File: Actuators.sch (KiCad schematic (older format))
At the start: 16 parts, among them J1 SERVO PWR, M1 Motor_Servo, M2 Motor_Servo, M3 Pump 1, M4 Pump 2, U6 DRV8847_TSSOP

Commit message: Upadate footprints, rough arrangement
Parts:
- removed L1: Solenoid 1, Connector_PinHeader_2.54mm:PinHeader_1x02_P2.54mm_Vertical, symbol Device:Electromagnetic_Actor
- removed L2: Solenoid 2, Connector_PinHeader_2.54mm:PinHeader_1x02_P2.54mm_Vertical, symbol Device:Electromagnetic_Actor
- removed M3: Pump 1, Connector_PinHeader_2.54mm:PinHeader_1x02_P2.54mm_Vertical, symbol Motor:Motor_DC
- removed M4: Pump 2, Connector_PinHeader_2.54mm:PinHeader_1x02_P2.54mm_Vertical, symbol Motor:Motor_DC
- added J3: Actuator1, Connector_Molex:Molex_PicoBlade_53261-0471_1x04-1MP_P1.25mm_Horizontal, symbol Connector_Generic:Conn_01x04
- added J4: Actuator2, Connector_Molex:Molex_PicoBlade_53261-0471_1x04-1MP_P1.25mm_Horizontal, symbol Connector_Generic:Conn_01x04
- C19: footprint Capacitor_THT:CP_Radial_D6.3mm_P2.50mm -> Capacitor_SMD:CP_Elec_5x5.8
- J1: value SERVO PWR -> SERVO DCDC 5V; footprint Connector_PinHeader_2.54mm:PinHeader_1x02_P2.54mm_Vertical -> Connector_PinHeader_2.54mm:PinHeader_1x03_P2.54mm_Vertical; symbol Connector_Generic:Conn_01x02 -> Connector_Generic:Conn_01x03
- M1, M2: footprint Connector_PinHeader_2.54mm:PinHeader_1x03_P2.54mm_Horizontal -> Connector_Molex:Molex_PicoBlade_53261-0371_1x03-1MP_P1.25mm_Horizontal
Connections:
- net +BATT: now also J1.1 (Pin_1)
- net GND: now also J3.2 (Pin_2), J3.4 (Pin_4), J4.2 (Pin_2), J4.4 (Pin_4)
- net at D3.1 (K), U6.2 (OUT1): now also J3.1 (Pin_1)
- net at D5.1 (K), U6.7 (OUT3): now also J4.1 (Pin_1)
- net at C17.1, M1.2 (+), M2.2 (+): now also J1.3 (Pin_3); no longer J1.1 (Pin_1)
- net at D4.1 (K), U6.4 (OUT2): now also J3.3 (Pin_3)
- net at D6.1 (K), U6.5 (OUT4): now also J4.3 (Pin_3)
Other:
- note added: "Pump 1"
- note added: "Pump 2"
- note added: "Solenoid 1"
- note added: "Solenoid 2"
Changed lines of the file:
@@
 Text HLabel 3850 2950 0    50   Input ~ 0
 SOLENOID_IN2
-$Comp
-L Motor:Motor_Servo M1
-U 1 1 5E37BD0B
-P 5000 5350
-F 0 "M1" H 5332 5415 50  0000 L CNN
-F 1 "Motor_Servo" H 5332 5324 50  0000 L CNN
-F 2 "Connector_PinHeader_2.54mm:PinHeader_1x03_P2.54mm_Horizontal" H 5000 5160 50  0001 C CNN
-F 3 "http://forums.parallax.com/uploads/attachments/46831/74481.png" H 5000 5160 50  0001 C CNN
-	1    5000 5350
-	1    0    0    -1
-$EndComp
-$Comp
-L Motor:Motor_Servo M2
-U 1 1 5E38464C
-P 5000 5900
-F 0 "M2" H 5332 5965 50  0000 L CNN
-F 1 "Motor_Servo" H 5332 5874 50  0000 L CNN
-F 2 "Connector_PinHeader_2.54mm:PinHeader_1x03_P2.54mm_Horizontal" H 5000 5710 50  0001 C CNN
-F 3 "http://forums.parallax.com/uploads/attachments/46831/74481.png" H 5000 5710 50  0001 C CNN
-	1    5000 5900
-	1    0    0    -1
-$EndComp
 Text HLabel 3850 2750 0    50   Input ~ 0
 SOLENOID_IN1
@@
 $EndComp
 $Comp
-L Connector_Generic:Conn_01x02 J1
+L Connector_Generic:Conn_01x03 J1
 U 1 1 5E3C2833
-P 2600 5350
-F 0 "J1" H 2518 5567 50  0000 C CNN
-F 1 "SERVO PWR" H 2518 5476 50  0000 C CNN
-F 2 "Connector_PinHeader_2.54mm:PinHeader_1x02_P2.54mm_Vertical" H 2600 5350 50  0001 C CNN
-F 3 "~" H 2600 5350 50  0001 C CNN
-	1    2600 5350
+P 2600 5250
+F 0 "J1" H 2600 5450 50  0000 C CNN
+F 1 "SERVO DCDC 5V" H 2600 5000 50  0000 C CNN
+F 2 "Connector_PinHeader_2.54mm:PinHeader_1x03_P2.54mm_Vertical" H 2600 5250 50  0001 C CNN
+F 3 "~" H 2600 5250 50  0001 C CNN
+	1    2600 5250
 	-1   0    0    -1
 $EndComp
 Wire Wire Line
-	2800 5450 3050 5450
-Wire Wire Line
-	3050 5450 3050 5650
+	2800 5250 3050 5250
+Wire Wire Line
+	3050 5250 3050 5650
 Wire Wire Line
 	3050 5650 3350 5650
@@
 	1    0    0    -1
 $EndComp
-$Comp
-L Motor:Motor_DC M3
-U 1 1 5E248EAA
-P 7450 2150
-F 0 "M3" V 7250 2100 50  0000 C CNN
-F 1 "Pump 1" V 7650 2100 39  0000 C CNN
-F 2 "Connector_PinHeader_2.54mm:PinHeader_1x02_P2.54mm_Vertical" H 7450 2060 50  0001 C CNN
-F 3 "~" H 7450 2060 50  0001 C CNN
-	1    7450 2150
-	1    0    0    -1
-$EndComp
-$Comp
-L Motor:Motor_DC M4
-U 1 1 5E2BC872
-P 7450 3900
-F 0 "M4" V 7250 3850 50  0000 C CNN
-F 1 "Pump 2" V 7650 3850 39  0000 C CNN
-F 2 "Connector_PinHeader_2.54mm:PinHeader_1x02_P2.54mm_Vertical" H 7450 3810 50  0001 C CNN
-F 3 "~" H 7450 3810 50  0001 C CNN
-	1    7450 3900
-	1    0    0    -1
-$EndComp
 Wire Wire Line
 	5250 2650 6600 2650
@@
 Connection ~ 7000 1950
 Wire Wire Line
-	7000 1950 7450 1950
-Wire Wire Line
 	7000 2350 7000 2450
 Wire Wire Line
@@
 Connection ~ 7000 3700
 Wire Wire Line
-	7000 3700 7450 3700
-Wire Wire Line
 	7000 4100 7000 4200
 Wire Wire Line
@@
 	7000 4600 7000 4500
 Connection ~ 7000 4500
-Wire Wire Line
-	7000 4500 7450 4500
 Wire Wire Line
 	7000 4900 7000 5000
@@
 	7000 3150 7000 3250
 Wire Wire Line
-	7000 2750 7450 2750
-Wire Wire Line
 	5250 2750 7000 2750
 Connection ~ 7000 2750
 Wire Wire Line
 	7000 2850 7000 2750
-$Comp
-L Device:Electromagnetic_Actor L1
-U 1 1 5E5DF558
-P 7450 3050
-F 0 "L1" H 7580 3146 50  0000 L CNN
-F 1 "Solenoid 1" H 7580 3055 50  0000 L CNN
-F 2 "Connector_PinHeader_2.54mm:PinHeader_1x02_P2.54mm_Vertical" V 7425 3150 50  0001 C CNN
-F 3 "~" V 7425 3150 50  0001 C CNN
-	1    7450 3050
-	1    0    0    -1
-$EndComp
-Wire Wire Line
-	7450 2750 7450 2850
-Wire Wire Line
-	7450 3150 7450 3250
-$Comp
-L Device:Electromagnetic_Actor L2
-U 1 1 5E5E309E
-P 7450 4800
-F 0 "L2" H 7580 4896 50  0000 L CNN
-F 1 "Solenoid 2" H 7580 4805 50  0000 L CNN
-F 2 "Connector_PinHeader_2.54mm:PinHeader_1x02_P2.54mm_Vertical" V 7425 4900 50  0001 C CNN
-F 3 "~" V 7425 4900 50  0001 C CNN
-	1    7450 4800
-	1    0    0    -1
-$EndComp
-Wire Wire Line
-	7450 4500 7450 4600
-Wire Wire Line
-	7450 4900 7450 5000
-Text Notes 7600 2650 0    50   ~ 0
+Text Notes 7650 2050 0    50   ~ 0
 Actuator 1\n(1A max)
 Wire Notes Line
@@
 Wire Notes Line
 	6800 3600 8050 3600
-Text Notes 7600 4400 0    50   ~ 0
+Text Notes 7600 3800 0    50   ~ 0
 Actuator 2\n(1A max)
 $Comp
@@
 F 0 "C19" H 5200 2250 50  0000 L CNN
 F 1 "22uF" H 5200 2150 50  0000 L CNN
-F 2 "Capacitor_THT:CP_Radial_D6.3mm_P2.50mm" H 5538 2050 50  0001 C CNN
+F 2 "Capacitor_SMD:CP_Elec_5x5.8" H 5538 2050 50  0001 C CNN
 F 3 "~" H 5500 2200 50  0001 C CNN
 	1    5500 2200
@@
 Text Notes 5200 2400 0    50   ~ 0
 ≥16V
+$Comp
+L Motor:Motor_Servo M2
+U 1 1 5E38464C
+P 5000 5900
+F 0 "M2" H 5332 5965 50  0000 L CNN
+F 1 "Motor_Servo" H 5332 5874 50  0000 L CNN
+F 2 "Connector_Molex:Molex_PicoBlade_53261-0371_1x03-1MP_P1.25mm_Horizontal" H 5000 5710 50  0001 C CNN
+F 3 "http://forums.parallax.com/uploads/attachments/46831/74481.png" H 5000 5710 50  0001 C CNN
+	1    5000 5900
+	1    0    0    -1
+$EndComp
+$Comp
+L Motor:Motor_Servo M1
+U 1 1 5E37BD0B
+P 5000 5350
+F 0 "M1" H 5332 5415 50  0000 L CNN
+F 1 "Motor_Servo" H 5332 5324 50  0000 L CNN
+F 2 "Connector_Molex:Molex_PicoBlade_53261-0371_1x03-1MP_P1.25mm_Horizontal" H 5000 5160 50  0001 C CNN
+F 3 "http://forums.parallax.com/uploads/attachments/46831/74481.png" H 5000 5160 50  0001 C CNN
+	1    5000 5350
+	1    0    0    -1
+$EndComp
+$Comp
+L Connector_Generic:Conn_01x04 J3
+U 1 1 5E485C32
+P 7750 2650
+F 0 "J3" H 7830 2642 50  0000 L CNN
+F 1 "Actuator1" H 7830 2551 50  0000 L CNN
+F 2 "Connector_Molex:Molex_PicoBlade_53261-0471_1x04-1MP_P1.25mm_Horizontal" H 7750 2650 50  0001 C CNN
+F 3 "~" H 7750 2650 50  0001 C CNN
+	1    7750 2650
+	1    0    0    -1
+$EndComp
+$Comp
+L Connector_Generic:Conn_01x04 J4
+U 1 1 5E486381
+P 7750 4400
+F 0 "J4" H 7830 4392 50  0000 L CNN
+F 1 "Actuator2" H 7830 4301 50  0000 L CNN
+F 2 "Connector_Molex:Molex_PicoBlade_53261-0471_1x04-1MP_P1.25mm_Horizontal" H 7750 4400 50  0001 C CNN
+F 3 "~" H 7750 4400 50  0001 C CNN
+	1    7750 4400
+	1    0    0    -1
+$EndComp
+Wire Wire Line
+	7550 1950 7550 2550
+Wire Wire Line
+	7000 1950 7550 1950
+Wire Wire Line
+	7450 2450 7450 2650
+Wire Wire Line
+	7450 2650 7550 2650
+Wire Wire Line
+	7000 2750 7550 2750
+Wire Wire Line
+	7550 2850 7450 2850
+Wire Wire Line
+	7450 2850 7450 3250
+Wire Wire Line
+	7000 4500 7550 4500
+Wire Wire Line
+	7550 4400 7450 4400
+Wire Wire Line
+	7450 4400 7450 4200
+Wire Wire Line
+	7550 4300 7550 3700
+Wire Wire Line
+	7000 3700 7550 3700
+Wire Wire Line
+	7550 4600 7450 4600
+Wire Wire Line
+	7450 4600 7450 5000
+Text Notes 7600 4050 0    50   ~ 0
+Pump 2
+Text Notes 7550 4850 0    50   ~ 0
+Solenoid 2
+Text Notes 7500 3100 0    50   ~ 0
+Solenoid 1
+Text Notes 7600 2350 0    50   ~ 0
+Pump 1
+$Comp
+L power:+BATT #PWR0111
+U 1 1 5E4B1181
+P 2800 5150
+F 0 "#PWR0111" H 2800 5000 50  0001 C CNN
+F 1 "+BATT" H 2815 5323 50  0000 C CNN
+F 2 "" H 2800 5150 50  0001 C CNN
+F 3 "" H 2800 5150 50  0001 C CNN
+	1    2800 5150
+	1    0    0    -1
+$EndComp
 $EndSCHEMATC

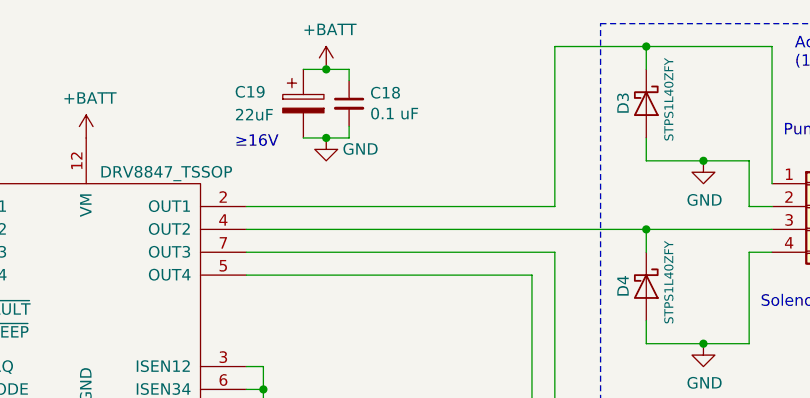
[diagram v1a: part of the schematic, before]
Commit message: Add digikey references for BOM
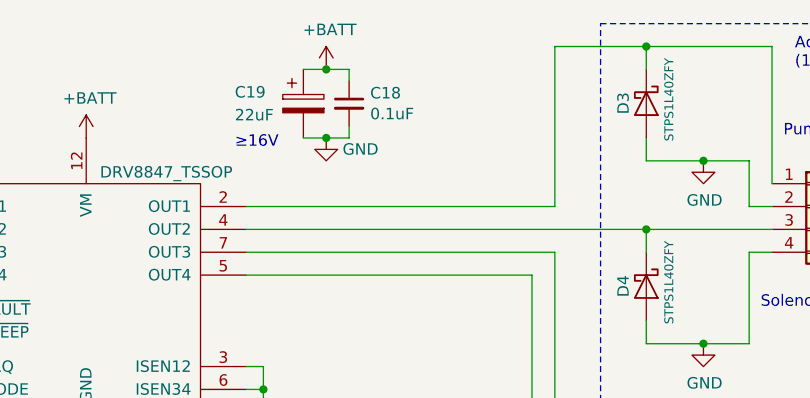
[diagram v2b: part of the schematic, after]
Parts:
- C17: digikey# (none) -> 399-7442-1-ND
- C18: value 0.1 uF -> 0.1uF; digikey# (none) -> 399-1283-1-ND
- C19: digikey# (none) -> PCE4240CT-ND
- D3, D4, D5, D6: Digikey 497-17153-1-ND -> (none); digikey# (none) -> 497-17153-1-ND
- J1: DNP (none) -> 1
- J3, J4: digikey# (none) -> WM7622CT-ND
- M1: digikey# (none) -> WM7621CT-ND
- R2: digikey# (none) -> 311-10KGRCT-ND
- U6: digikey# (none) -> 296-53425-1-ND
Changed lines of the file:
@@
 EESchema Schematic File Version 4
-LIBS:actuator-board-cache
 EELAYER 30 0
 EELAYER END
@@
 F 2 "Capacitor_SMD:C_1206_3216Metric" H 3388 5350 50  0001 C CNN
 F 3 "~" H 3350 5500 50  0001 C CNN
+F 4 "399-7442-1-ND" H 3350 5500 50  0001 C CNN "digikey#"
 	1    3350 5500
 	1    0    0    -1
@@
 F 2 "Connector_PinHeader_2.54mm:PinHeader_1x03_P2.54mm_Vertical" H 2600 5250 50  0001 C CNN
 F 3 "~" H 2600 5250 50  0001 C CNN
+F 4 "1" H 2600 5250 50  0001 C CNN "DNP"
 	1    2600 5250
 	-1   0    0    -1
@@
 F 2 "Diode_SMD:D_SOD-123F" H 7000 2200 50  0001 C CNN
 F 3 "https://www.st.com/resource/en/datasheet/stps1l40-y.pdf" H 7000 2200 50  0001 C CNN
-F 4 "497-17153-1-ND" V 7000 2200 50  0001 C CNN "Digikey"
+F 4 "497-17153-1-ND" V 7000 2200 50  0001 C CNN "digikey#"
 	1    7000 2200
 	0    1    1    0
@@
 F 2 "Diode_SMD:D_SOD-123F" H 7000 3950 50  0001 C CNN
 F 3 "https://www.st.com/resource/en/datasheet/stps1l40-y.pdf" H 7000 3950 50  0001 C CNN
-F 4 "497-17153-1-ND" V 7000 3950 50  0001 C CNN "Digikey"
+F 4 "497-17153-1-ND" V 7000 3950 50  0001 C CNN "digikey#"
 	1    7000 3950
 	0    1    1    0
@@
 F 2 "Diode_SMD:D_SOD-123F" H 7000 4750 50  0001 C CNN
 F 3 "https://www.st.com/resource/en/datasheet/stps1l40-y.pdf" H 7000 4750 50  0001 C CNN
-F 4 "497-17153-1-ND" V 7000 4750 50  0001 C CNN "Digikey"
+F 4 "497-17153-1-ND" V 7000 4750 50  0001 C CNN "digikey#"
 	1    7000 4750
 	0    1    1    0
@@
 F 2 "Diode_SMD:D_SOD-123F" H 7000 3000 50  0001 C CNN
 F 3 "https://www.st.com/resource/en/datasheet/stps1l40-y.pdf" H 7000 3000 50  0001 C CNN
-F 4 "497-17153-1-ND" V 7000 3000 50  0001 C CNN "Digikey"
+F 4 "497-17153-1-ND" V 7000 3000 50  0001 C CNN "digikey#"
 	1    7000 3000
 	0    1    1    0
@@
 F 2 "Package_SO:TSSOP-16_4.4x5mm_P0.65mm" H 4550 3000 50  0001 C CNN
 F 3 "http://www.ti.com/lit/ds/symlink/drv8847.pdf" H 4550 3000 50  0001 C CNN
+F 4 "296-53425-1-ND" H 4550 3050 50  0001 C CNN "digikey#"
 	1    4550 3050
 	1    0    0    -1
@@
 P 5700 2200
 F 0 "C18" H 5792 2246 50  0000 L CNN
-F 1 "0.1 uF" H 5792 2155 50  0000 L CNN
+F 1 "0.1uF" H 5792 2155 50  0000 L CNN
 F 2 "Capacitor_SMD:C_0603_1608Metric" H 5700 2200 50  0001 C CNN
 F 3 "~" H 5700 2200 50  0001 C CNN
+F 4 "399-1283-1-ND" H 5700 2200 50  0001 C CNN "digikey#"
 	1    5700 2200
 	1    0    0    -1
@@
 F 2 "Capacitor_SMD:CP_Elec_5x5.8" H 5538 2050 50  0001 C CNN
 F 3 "~" H 5500 2200 50  0001 C CNN
+F 4 "PCE4240CT-ND" H 5500 2200 50  0001 C CNN "digikey#"
 	1    5500 2200
 	1    0    0    -1
@@
 F 2 "Resistor_SMD:R_0603_1608Metric" H 3400 3300 50  0001 C CNN
 F 3 "~" H 3400 3300 50  0001 C CNN
+F 4 "311-10KGRCT-ND" H 3400 3300 50  0001 C CNN "digikey#"
 	1    3400 3300
 	1    0    0    -1
@@
 F 2 "Connector_Molex:Molex_PicoBlade_53261-0371_1x03-1MP_P1.25mm_Horizontal" H 5000 5160 50  0001 C CNN
 F 3 "http://forums.parallax.com/uploads/attachments/46831/74481.png" H 5000 5160 50  0001 C CNN
+F 4 "WM7621CT-ND" H 5000 5350 50  0001 C CNN "digikey#"
 	1    5000 5350
 	1    0    0    -1
@@
 F 2 "Connector_Molex:Molex_PicoBlade_53261-0471_1x04-1MP_P1.25mm_Horizontal" H 7750 2650 50  0001 C CNN
 F 3 "~" H 7750 2650 50  0001 C CNN
+F 4 "WM7622CT-ND" H 7750 2650 50  0001 C CNN "digikey#"
 	1    7750 2650
 	1    0    0    -1
@@
 F 2 "Connector_Molex:Molex_PicoBlade_53261-0471_1x04-1MP_P1.25mm_Horizontal" H 7750 4400 50  0001 C CNN
 F 3 "~" H 7750 4400 50  0001 C CNN
+F 4 "WM7622CT-ND" H 7750 4400 50  0001 C CNN "digikey#"
 	1    7750 4400
 	1    0    0    -1
